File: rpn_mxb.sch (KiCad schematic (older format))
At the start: 8 parts, among them J1 Conn_01x16_Female, J2 Conn_01x05_Female, U1 PIC18F25K40_ISS, Y1 Crystal

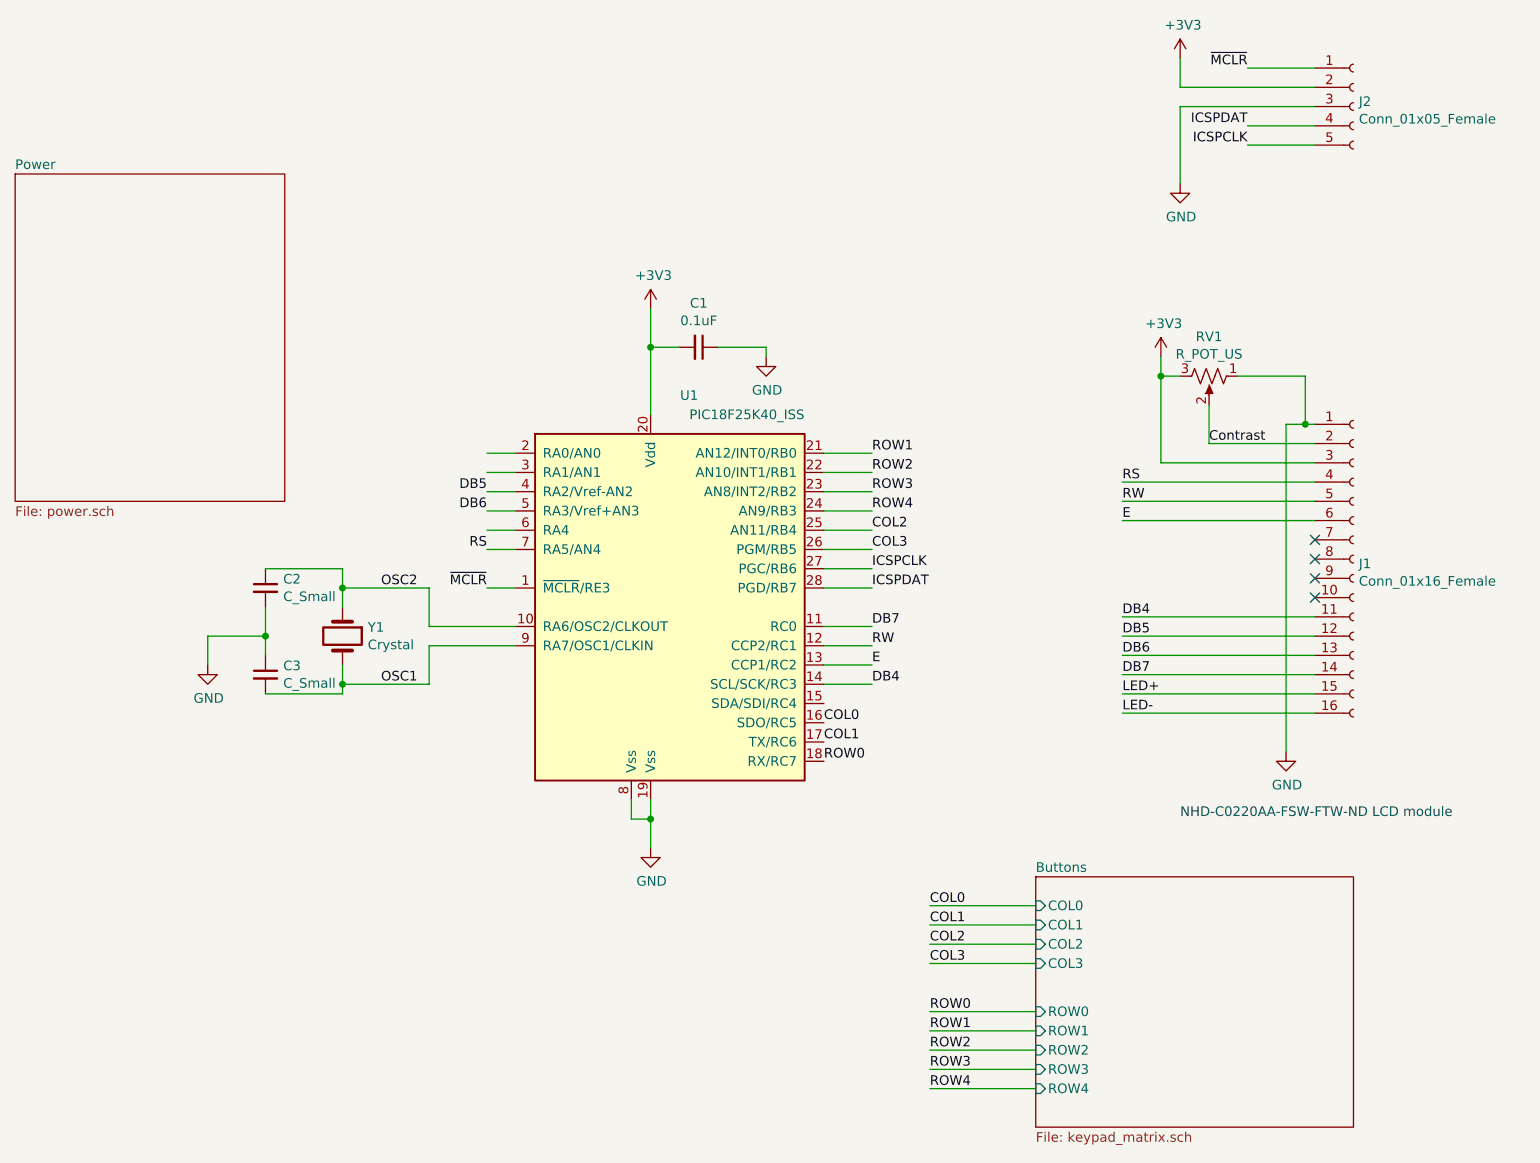
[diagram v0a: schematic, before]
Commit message: DFM version
Add ability for microcontroller to enable/disable backlight, fix bug
with where BATT net comes from, create gerbers to submit to DFM.
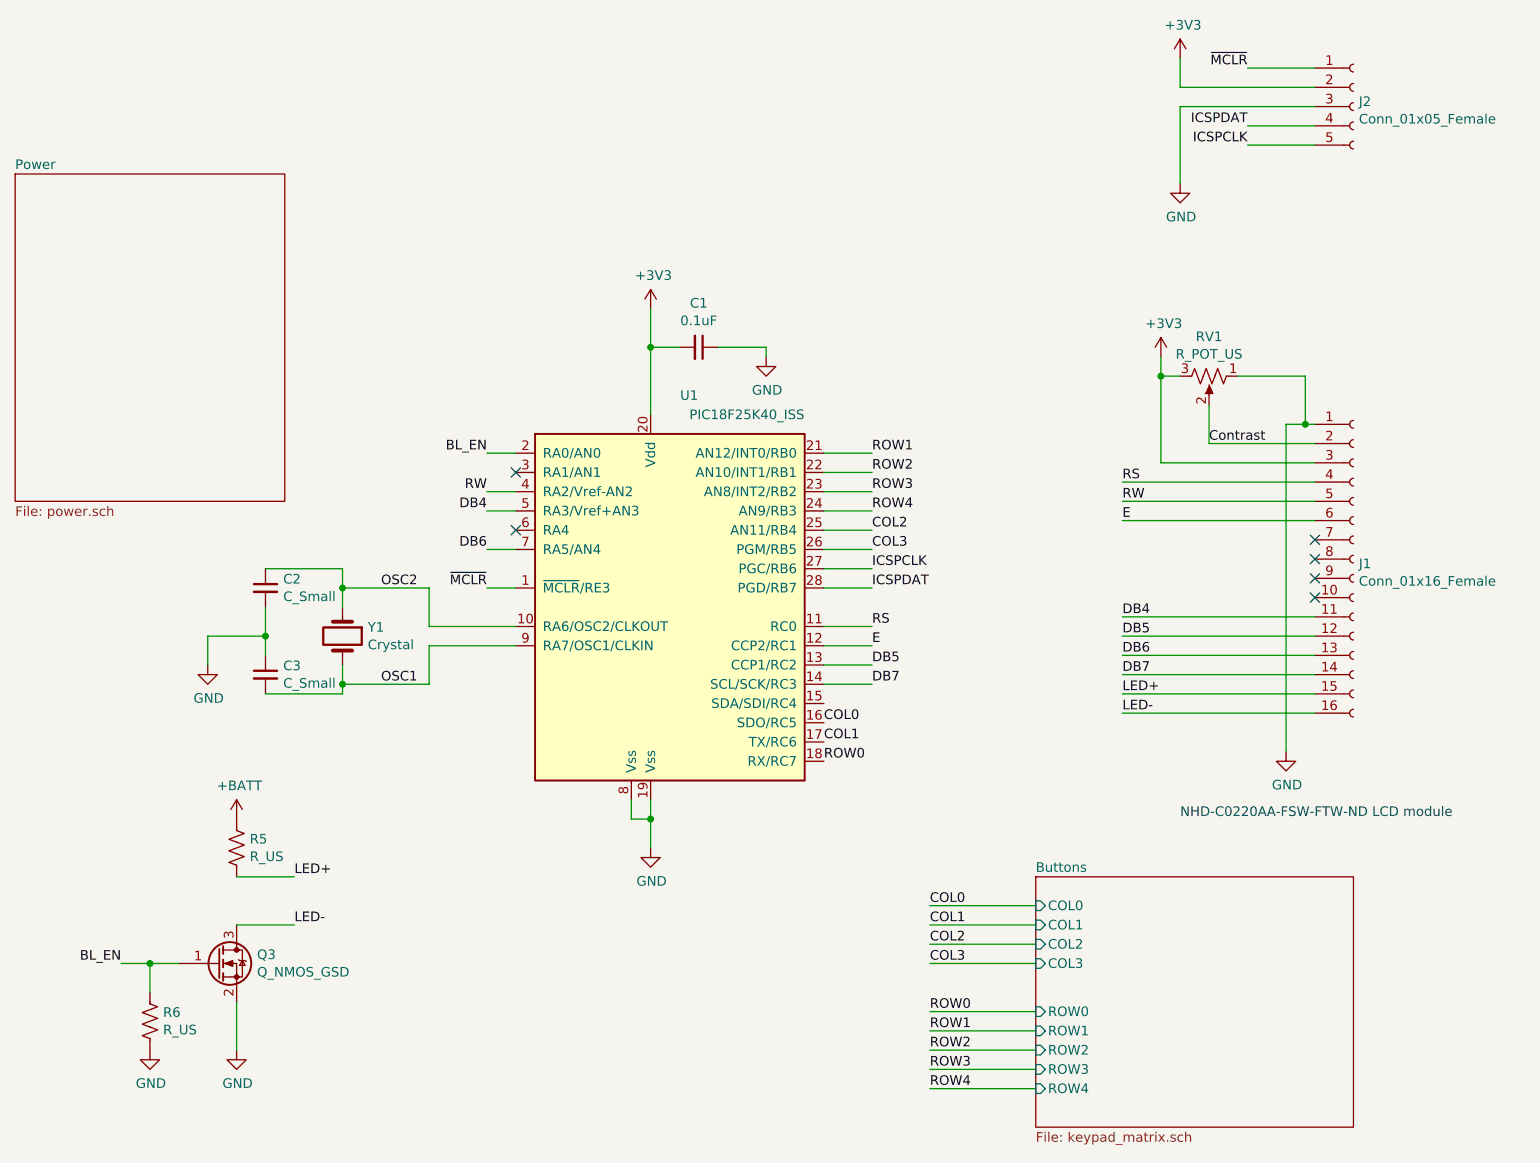
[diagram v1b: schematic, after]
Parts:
- added Q3: Q_NMOS_GSD, Package_TO_SOT_SMD:SOT-23_Handsoldering, symbol Device:Q_NMOS_GSD
- added R5, R6: R_US, Resistor_SMD:R_0805_2012Metric_Pad1.15x1.40mm_HandSolder, symbol Device:R_US
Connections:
- net labels added: +BATT, BL_EN
- wire segments 80 -> 84
- no-connect marks 4 -> 6
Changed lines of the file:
@@
 EESchema Schematic File Version 4
-LIBS:rpn_mxb-cache
-EELAYER 29 0
+EELAYER 30 0
 EELAYER END
 $Descr A4 11693 8268
@@
 	9500 2400 9500 2300
 Wire Wire Line
-	10300 2950 9300 2950
-Wire Wire Line
 	10300 3050 9300 3050
 Wire Wire Line
@@
 Wire Wire Line
 	6850 4700 6850 4600
+Text Label 6000 3000 2    50   ~ 0
+RW
+Text Label 8000 3800 0    50   ~ 0
+E
+Wire Wire Line
+	7750 2800 8000 2800
+Wire Wire Line
+	7750 2900 8000 2900
+Wire Wire Line
+	7750 3000 8000 3000
+Text Label 6000 3100 2    50   ~ 0
+DB4
 Text Label 6000 3300 2    50   ~ 0
-RS
-Text Label 8000 3800 0    50   ~ 0
-RW
-Text Label 8000 3900 0    50   ~ 0
-E
-Wire Wire Line
-	7750 2800 8000 2800
-Wire Wire Line
-	7750 2900 8000 2900
-Wire Wire Line
-	7750 3000 8000 3000
-Text Label 8000 4000 0    50   ~ 0
-DB4
-Text Label 6000 3100 2    50   ~ 0
 DB6
 Wire Wire Line
@@
 	1    0    0    -1
 $EndComp
-Text Label 8000 3700 0    50   ~ 0
+Text Label 8000 4000 0    50   ~ 0
 DB7
 Text Label 8300 5150 0    50   ~ 0
@@
 	6000 2800 6150 2800
 Wire Wire Line
-	6150 2900 6000 2900
-Wire Wire Line
 	6000 3000 6150 3000
 Wire Wire Line
 	6150 3100 6000 3100
-Wire Wire Line
-	6000 3200 6150 3200
 Wire Wire Line
 	6150 3300 6000 3300
@@
 Text Label 5450 3500 0    50   ~ 0
 OSC2
-Text Label 6000 3000 2    50   ~ 0
+Text Label 8000 3900 0    50   ~ 0
 DB5
+Wire Wire Line
+	10300 2950 9300 2950
+$Comp
+L Device:Q_NMOS_GSD Q3
+U 1 1 5E285F1D
+P 4600 5450
+F 0 "Q3" H 4806 5496 50  0000 L CNN
+F 1 "Q_NMOS_GSD" H 4806 5405 50  0000 L CNN
+F 2 "Package_TO_SOT_SMD:SOT-23_Handsoldering" H 4800 5550 50  0001 C CNN
+F 3 "~" H 4600 5450 50  0001 C CNN
+	1    4600 5450
+	1    0    0    -1
+$EndComp
+$Comp
+L power:GND #PWR06
+U 1 1 5E2866B1
+P 4700 5900
+F 0 "#PWR06" H 4700 5650 50  0001 C CNN
+F 1 "GND" H 4705 5727 50  0000 C CNN
+F 2 "" H 4700 5900 50  0001 C CNN
+F 3 "" H 4700 5900 50  0001 C CNN
+	1    4700 5900
+	1    0    0    -1
+$EndComp
+$Comp
+L power:+BATT #PWR04
+U 1 1 5E286FED
+P 4700 4700
+F 0 "#PWR04" H 4700 4550 50  0001 C CNN
+F 1 "+BATT" H 4715 4873 50  0000 C CNN
+F 2 "" H 4700 4700 50  0001 C CNN
+F 3 "" H 4700 4700 50  0001 C CNN
+	1    4700 4700
+	1    0    0    -1
+$EndComp
+$Comp
+L Device:R_US R5
+U 1 1 5E287745
+P 4700 4850
+F 0 "R5" H 4768 4896 50  0000 L CNN
+F 1 "R_US" H 4768 4805 50  0000 L CNN
+F 2 "Resistor_SMD:R_0805_2012Metric_Pad1.15x1.40mm_HandSolder" V 4740 4840 50  0001 C CNN
+F 3 "~" H 4700 4850 50  0001 C CNN
+	1    4700 4850
+	1    0    0    -1
+$EndComp
+$Comp
+L Device:R_US R6
+U 1 1 5E28B79D
+P 4250 5750
+F 0 "R6" H 4318 5796 50  0000 L CNN
+F 1 "R_US" H 4318 5705 50  0000 L CNN
+F 2 "Resistor_SMD:R_0805_2012Metric_Pad1.15x1.40mm_HandSolder" V 4290 5740 50  0001 C CNN
+F 3 "~" H 4250 5750 50  0001 C CNN
+	1    4250 5750
+	1    0    0    -1
+$EndComp
+$Comp
+L power:GND #PWR05
+U 1 1 5E28C9E7
+P 4250 5900
+F 0 "#PWR05" H 4250 5650 50  0001 C CNN
+F 1 "GND" H 4255 5727 50  0000 C CNN
+F 2 "" H 4250 5900 50  0001 C CNN
+F 3 "" H 4250 5900 50  0001 C CNN
+	1    4250 5900
+	1    0    0    -1
+$EndComp
+Wire Wire Line
+	4700 5900 4700 5650
+Wire Wire Line
+	4250 5600 4250 5450
+Wire Wire Line
+	4250 5450 4400 5450
+Text Label 4100 5450 2    50   ~ 0
+BL_EN
+Wire Wire Line
+	4100 5450 4250 5450
+Connection ~ 4250 5450
+Text Label 6000 2800 2    50   ~ 0
+BL_EN
+Text Label 8000 3700 0    50   ~ 0
+RS
+Text Label 5000 5250 0    50   ~ 0
+LED-
+Text Label 5000 5000 0    50   ~ 0
+LED+
+Wire Wire Line
+	5000 5000 4700 5000
+Wire Wire Line
+	4700 5250 5000 5250
+NoConn ~ 6150 3200
+NoConn ~ 6150 2900
 $EndSCHEMATC

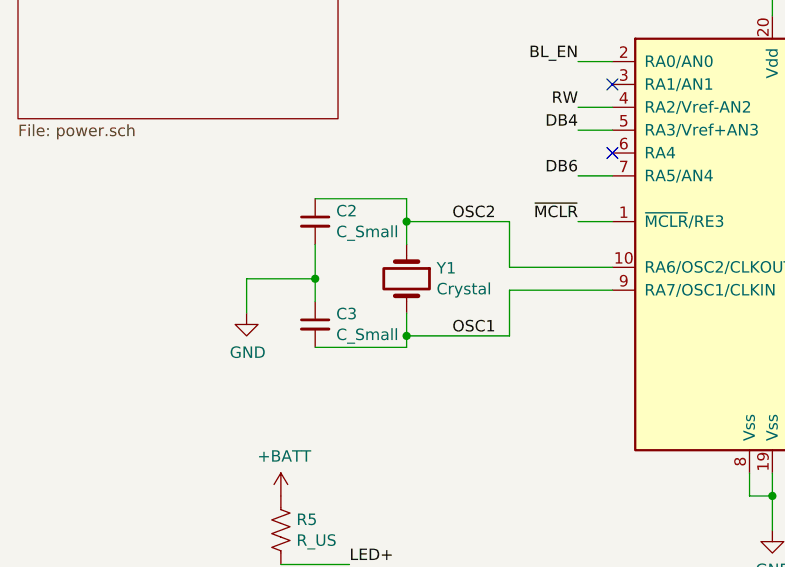
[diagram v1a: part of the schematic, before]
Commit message: Add TODO comments to schematic based on assemby epiphanies
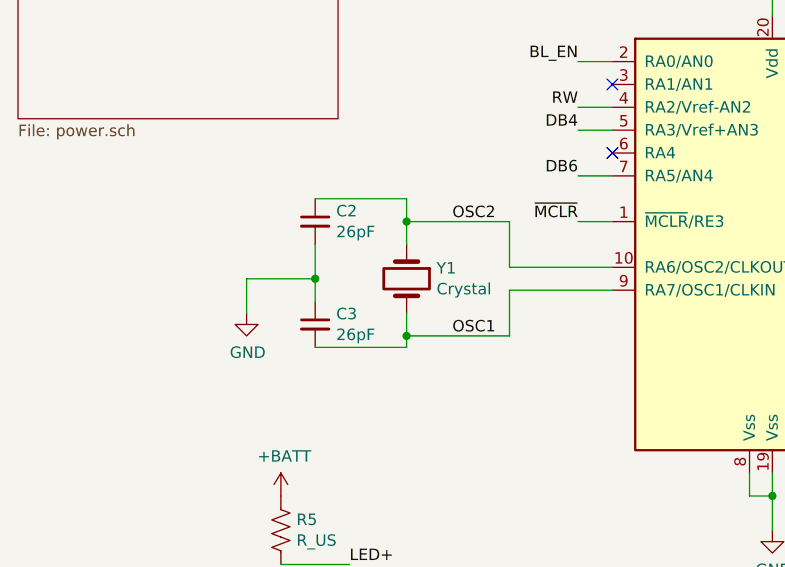
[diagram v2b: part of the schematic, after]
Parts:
- C2, C3: value C_Small -> 26pF
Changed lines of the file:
@@
 P 4850 3500
 F 0 "C2" H 4942 3546 50  0000 L CNN
-F 1 "C_Small" H 4942 3455 50  0000 L CNN
+F 1 "26pF" H 4942 3455 50  0000 L CNN
 F 2 "Capacitor_SMD:C_0805_2012Metric_Pad1.15x1.40mm_HandSolder" H 4850 3500 50  0001 C CNN
 F 3 "~" H 4850 3500 50  0001 C CNN
@@
 P 4850 3950
 F 0 "C3" H 4942 3996 50  0000 L CNN
-F 1 "C_Small" H 4942 3905 50  0000 L CNN
+F 1 "26pF" H 4942 3905 50  0000 L CNN
 F 2 "Capacitor_SMD:C_0805_2012Metric_Pad1.15x1.40mm_HandSolder" H 4850 3950 50  0001 C CNN
 F 3 "~" H 4850 3950 50  0001 C CNN
